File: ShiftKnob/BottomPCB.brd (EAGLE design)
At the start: 37.8 x 40.2 mm, 40 parts, among them IC2 UA78M05DCY, J1 AVR_SPI_PRG_6PTH, Q1 16MHz, Q2 MOSFET-NCHANNELSMD, Q3 MOSFET-PCHANNELSMD, Q4 MOSFET-NCHANNELSMD, Q5 MOSFET-NCHANNELSMD, Q6 MOSFET-NCHANNELSMD, U1 ATMEGA328, U3 FT232RL-BASICSSOP

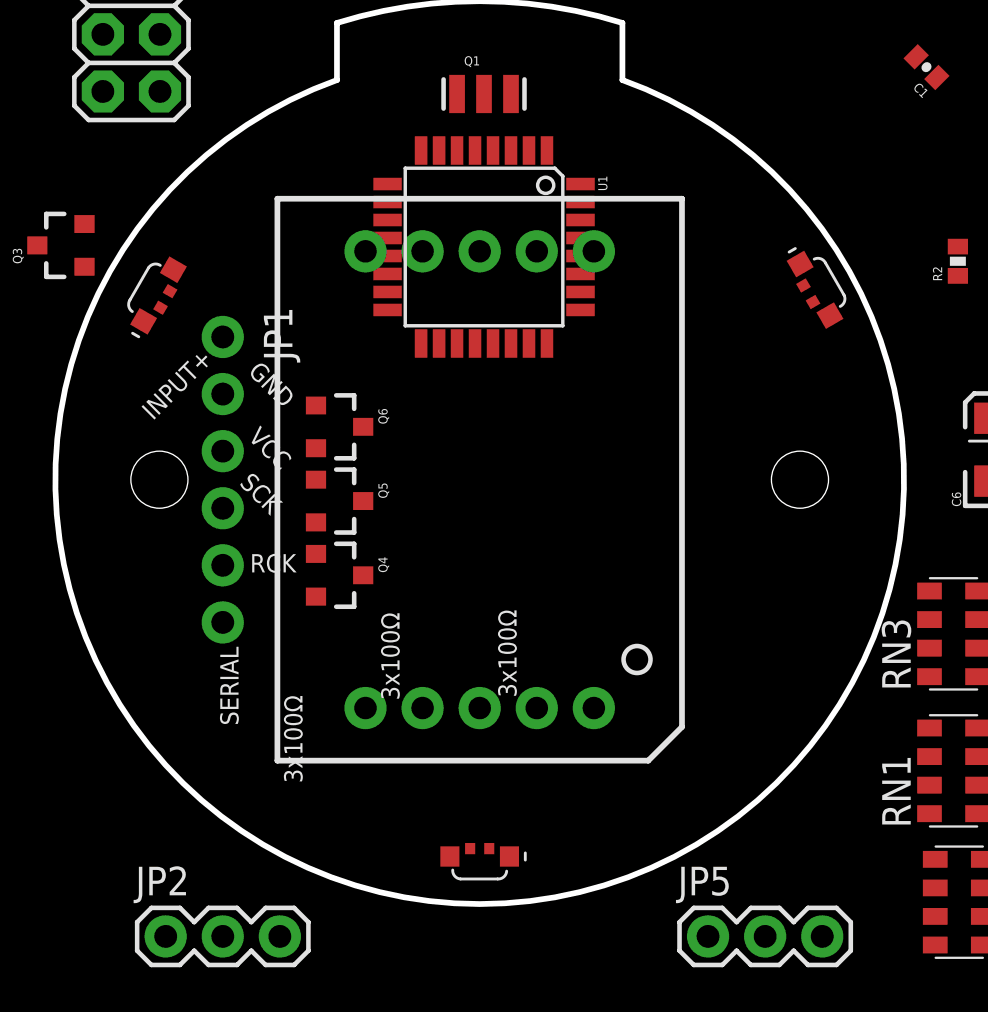
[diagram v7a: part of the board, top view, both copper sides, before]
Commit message: remove 6 pin header. add (2) 4 pin headers and place in the correct location to match TopPCB.
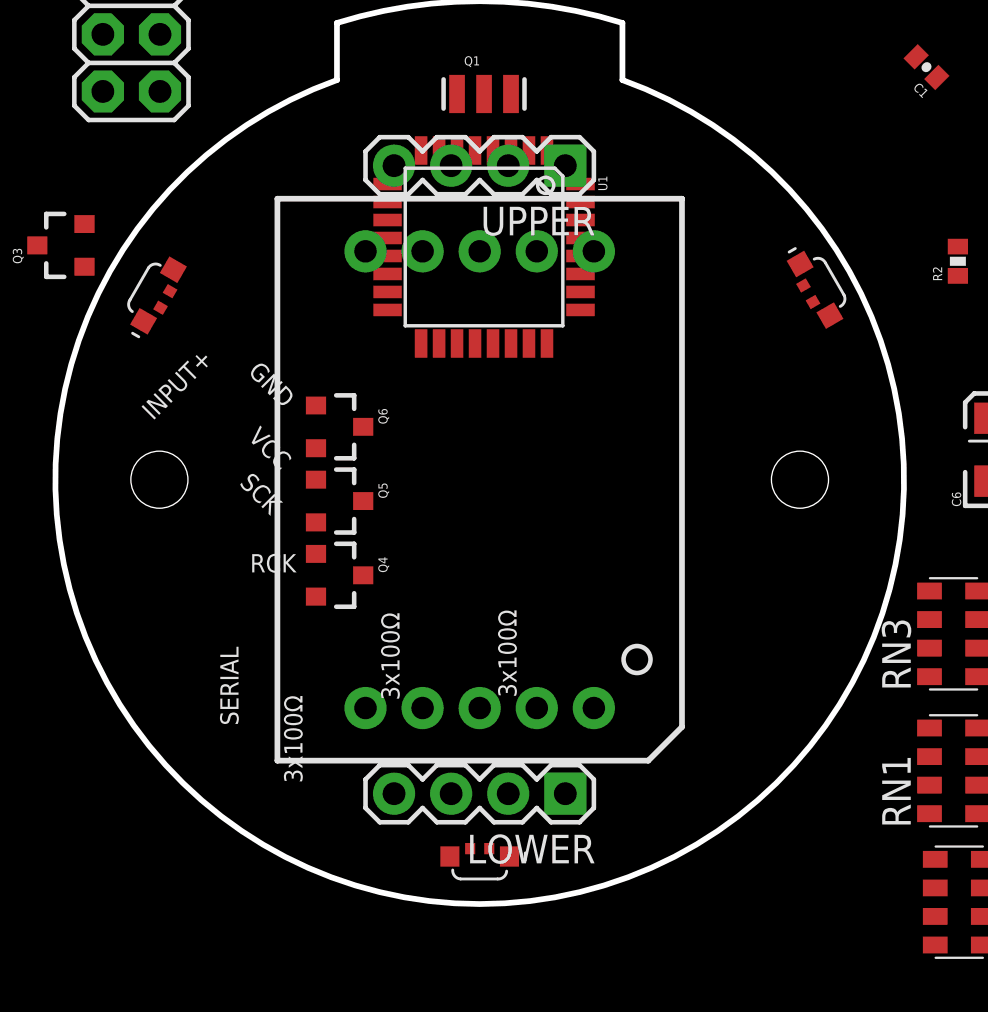
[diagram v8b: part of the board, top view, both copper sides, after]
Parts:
- removed JP1: 6 PIN 90degree Header, SparkFun-Connectors:1X06
- removed JP2, JP5: (no value), SparkFun-Connectors:1X03
- added LOWER, UPPER: (no value), SparkFun-Connectors:1X04
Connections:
- removed net N$20: JP2.2
- removed net N$26: JP2.1
- removed net N$27: JP5.3
- removed net N$28: JP5.2
- removed net N$29: JP5.1
- removed net N$3: JP2.3
- net D4/SERIAL: now also LOWER.2; no longer JP1.6
- net D7/RCK: now also LOWER.3; no longer JP1.5
- net D8/SCK: now also LOWER.4; no longer JP1.4
- net GND: now also LOWER.1, UPPER.1, UPPER.3; no longer JP1.2
- net INPUT+: now also UPPER.2; no longer JP1.1
- net VCC: now also UPPER.4; no longer JP1.3
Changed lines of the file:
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@@
 </autorouter>
 <elements>
-<element name="JP1" library="SparkFun-Connectors" package="1X06" value="6 PIN 90degree Header" x="10.16" y="27.94" rot="R270"/>
 <element name="R2" library="SparkFun" package="0402-RES" value="10K" x="42.865" y="31.308" rot="R90"/>
 <element name="C3" library="SparkFun" package="0402-CAP" value="0.1uF" x="46.04" y="37.272" rot="R315"/>
@@
 <element name="BUTTON" library="FORD_frames" package="BUTTON_RIGHTANGLE" value="BUTTON_RIGHTANGLE_SMD" x="67.31" y="20.32" rot="R90"/>
 <element name="U$2" library="SparkFun-Displays" package="7-SEGMENT-1&quot;PTH" value="7-SEGMENT-DISPLAY-1&quot;-RED" x="21.59" y="21.59"/>
-<element name="JP2" library="SparkFun-Connectors" package="1X03" value="" x="7.62" y="1.27"/>
-<element name="JP5" library="SparkFun-Connectors" package="1X03" value="" x="31.75" y="1.27"/>
+<element name="UPPER" library="SparkFun-Connectors" package="1X04" value="" x="25.4" y="35.56" rot="R180"/>
+<element name="LOWER" library="SparkFun-Connectors" package="1X04" value="" x="25.4" y="7.62" rot="R180"/>
 </elements>
 <signals>
 <signal name="INPUT+">
-<contactref element="JP1" pad="1"/>
 <contactref element="Q3" pad="3"/>
-<wire x1="1.9074" y1="32.0142" x2="10.16" y2="27.94" width="0" layer="19" extent="1-1"/>
+<contactref element="UPPER" pad="2"/>
+<wire x1="22.86" y1="35.56" x2="1.9074" y2="32.0142" width="0" layer="19" extent="1-1"/>
 </signal>
 <signal name="GND" airwireshidden="yes">
-<contactref element="JP1" pad="2"/>
 <contactref element="C3" pad="1"/>
 <contactref element="C1" pad="1"/>
@@
 <contactref element="C4" pad="1"/>
 <contactref element="BUTTON" pad="PIN1"/>
+<contactref element="UPPER" pad="3"/>
+<contactref element="UPPER" pad="1"/>
+<contactref element="LOWER" pad="1"/>
 <wire x1="75.255" y1="45.366" x2="74.605" y2="52.678" width="0" layer="19" extent="16-16"/>
 <wire x1="77.205" y1="45.366" x2="75.255" y2="45.366" width="0" layer="19" extent="16-16"/>
@@
 <wire x1="41.92761875" y1="39.484378125" x2="45.580378125" y2="37.73161875" width="0" layer="19" extent="1-1"/>
 <wire x1="50.8712" y1="3.5314" x2="50.5562" y2="18.354" width="0" layer="19" extent="1-1"/>
+<wire x1="20.32" y1="35.56" x2="50.8712" y2="3.5314" width="0" layer="19" extent="1-1"/>
+<wire x1="25.4" y1="35.56" x2="20.32" y2="35.56" width="0" layer="19" extent="1-1"/>
 <wire x1="22.983" y1="36.2356" x2="41.92761875" y2="39.484378125" width="0" layer="19" extent="1-1"/>
 <wire x1="21.383" y1="36.2356" x2="22.983" y2="36.2356" width="0" layer="19" extent="1-1"/>
@@
 <wire x1="14.306" y1="19.69" x2="14.306" y2="22.992" width="0" layer="19" extent="1-1"/>
 <wire x1="14.306" y1="16.388" x2="14.306" y2="19.69" width="0" layer="19" extent="1-1"/>
-<wire x1="10.16" y1="25.4" x2="14.306" y2="22.992" width="0" layer="19" extent="1-1"/>
-<wire x1="7.366" y1="38.862" x2="10.16" y2="25.4" width="0" layer="19" extent="1-1"/>
+<wire x1="7.366" y1="38.862" x2="21.383" y2="36.2356" width="0" layer="19" extent="1-1"/>
+<wire x1="25.4" y1="7.62" x2="14.306" y2="16.388" width="0" layer="19" extent="1-1"/>
 </signal>
 <signal name="VCC">
-<contactref element="JP1" pad="3"/>
 <contactref element="R2" pad="2"/>
 <contactref element="C3" pad="2"/>
@@
 <contactref element="C5" pad="1"/>
 <contactref element="C6" pad="A"/>
+<contactref element="UPPER" pad="4"/>
 <wire x1="46.421" y1="32.212" x2="46.49961875" y2="36.812378125" width="0" layer="19" extent="1-1"/>
 <wire x1="42.865" y1="31.958" x2="46.421" y2="32.212" width="0" layer="19" extent="1-1"/>
@@
 <wire x1="53.3044" y1="6.3298" x2="49.9035" y2="8.526896875" width="0" layer="19" extent="1-16"/>
 <wire x1="60.1922" y1="8.5412" x2="53.3044" y2="6.3298" width="0" layer="19" extent="1-16"/>
+<wire x1="17.78" y1="35.56" x2="49.9035" y2="8.526896875" width="0" layer="19" extent="16-16"/>
 <wire x1="22.183" y1="36.2356" x2="42.865" y2="31.958" width="0" layer="19" extent="1-1"/>
 <wire x1="20.583" y1="36.2356" x2="22.183" y2="36.2356" width="0" layer="19" extent="1-1"/>
 <wire x1="19.783" y1="27.6504" x2="20.583" y2="36.2356" width="0" layer="19" extent="1-1"/>
-<wire x1="10.16" y1="22.86" x2="19.783" y2="27.6504" width="0" layer="19" extent="1-1"/>
-<wire x1="4.0074" y1="32.9642" x2="10.16" y2="22.86" width="0" layer="19" extent="1-1"/>
-<wire x1="7.366" y1="43.942" x2="4.0074" y2="32.9642" width="0" layer="19" extent="1-1"/>
+<wire x1="7.366" y1="43.942" x2="20.583" y2="36.2356" width="0" layer="19" extent="1-1"/>
+<wire x1="4.0074" y1="32.9642" x2="7.366" y2="43.942" width="0" layer="19" extent="1-1"/>
 </signal>
 <signal name="AREF">
@@
 <signal name="D8/SCK">
 <contactref element="U1" pad="12"/>
-<contactref element="JP1" pad="4"/>
-<wire x1="10.16" y1="20.32" x2="17.4904" y2="32.343" width="0" layer="19" extent="1-1"/>
+<contactref element="LOWER" pad="4"/>
+<wire x1="17.78" y1="7.62" x2="17.4904" y2="32.343" width="0" layer="19" extent="1-1"/>
 </signal>
 <signal name="A5">
@@
 <signal name="D4/SERIAL">
 <contactref element="U1" pad="2"/>
-<contactref element="JP1" pad="6"/>
-<wire x1="10.16" y1="15.24" x2="23.783" y2="36.2356" width="0" layer="19" extent="1-1"/>
+<contactref element="LOWER" pad="2"/>
+<wire x1="22.86" y1="7.62" x2="23.783" y2="36.2356" width="0" layer="19" extent="1-1"/>
 </signal>
 <signal name="D5/MOTOR">
@@
 <signal name="D7/RCK">
 <contactref element="U1" pad="11"/>
-<contactref element="JP1" pad="5"/>
-<wire x1="10.16" y1="17.78" x2="17.4904" y2="33.143" width="0" layer="19" extent="1-1"/>
+<contactref element="LOWER" pad="3"/>
+<wire x1="20.32" y1="7.62" x2="17.4904" y2="33.143" width="0" layer="19" extent="1-1"/>
 </signal>
 <signal name="D10">
@@
 <wire x1="22.02" y1="5.176" x2="7.38810625" y2="29.23660625" width="0" layer="19" extent="1-1"/>
 </signal>
-<signal name="N$3">
-<contactref element="JP2" pad="3"/>
-</signal>
-<signal name="N$20">
-<contactref element="JP2" pad="2"/>
-</signal>
-<signal name="N$26">
-<contactref element="JP2" pad="1"/>
-</signal>
-<signal name="N$27">
-<contactref element="JP5" pad="3"/>
-</signal>
-<signal name="N$28">
-<contactref element="JP5" pad="2"/>
-</signal>
-<signal name="N$29">
-<contactref element="JP5" pad="1"/>
-</signal>
 </signals>
